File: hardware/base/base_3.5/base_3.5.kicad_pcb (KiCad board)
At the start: 2 copper layers, 82.5 x 17 mm, 9 parts, among them IC1 single_pad_smd, IC2 single_pad_smd, J1 Conn 1, J2 Conn 2

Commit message: base 3.5 update
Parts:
- removed GND (x2): single_pad_smd, cycfi_library:single-pad-3x2
- removed IC1, IC2, OC1, OC2: single_pad_smd, cycfi_library:single-pad-2x2-th
- added J3: Conn_01x03, cycfi_library:xr2-coil-connector, F.Cu at (125.0, 52.0)
- added J4: Conn_01x03, cycfi_library:xr2-coil-connector, F.Cu at (125.0, 58.5)
- moved J2 0.30 mm to (153.1, 55.2)
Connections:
- net /ic2 renamed /OC2
- net /oc1 renamed /OC1
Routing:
- net GND: track 88.3 -> 9.22 mm, vias 6 -> 2
- net /ic1: track 34.3 -> 0.00 mm
- net /OC2: track 10.2 -> 32.6 mm
- net /IC1: track 0.00 -> 10.2 mm
- net /OC1: track 50.5 -> 42.8 mm
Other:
- board size 82.5 x 17 mm -> 82.4 x 17 mm
- board text removed: "IC1"
- board text removed: "IC2"
- board text removed: "OC1"
- board text removed: "OC2"

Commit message: 3.0 and 3.5 base updated
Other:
- board size 82.4 x 17 mm -> 82.5 x 17 mm

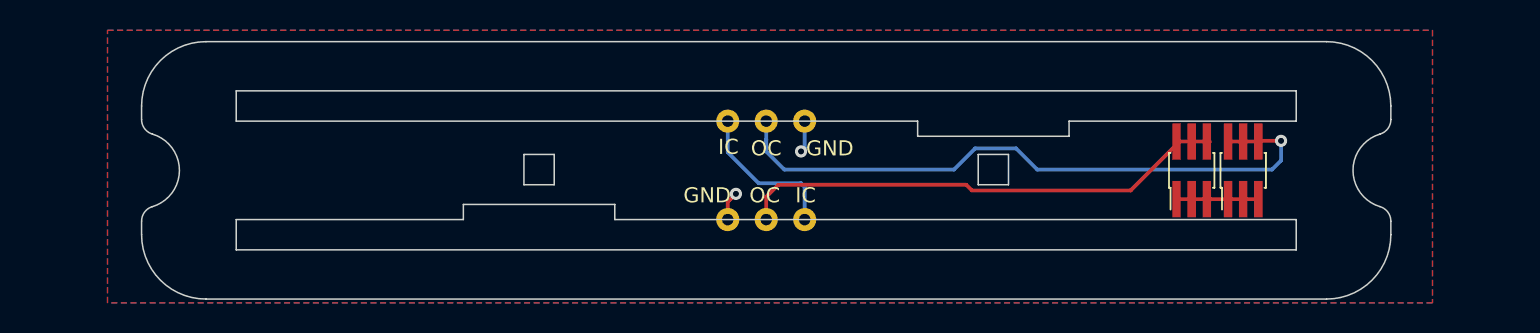
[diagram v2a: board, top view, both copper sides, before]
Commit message: Copied 3.3 to 3.5 and 4.0
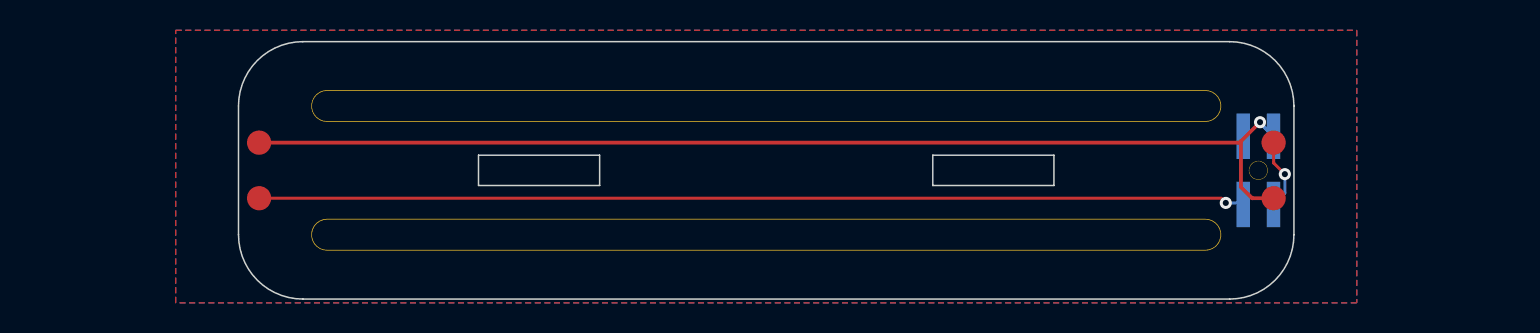
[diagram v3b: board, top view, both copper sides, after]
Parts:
- removed J2: Conn 2, cycfi_library:pin_header_2x3p_1.00mm_smd_vertical
- removed J3, J4: Conn_01x03, cycfi_library:xr2-coil-connector
- added H5: single_pad, xr_spectra_library:rail_slot_3.3, F.Cu at (125.0, 51.0)
- added H6: single_pad, xr_spectra_library:rail_slot_3.3, F.Cu at (125.0, 59.5)
- added IC1: single_pad, cycfi_library:single-pad-1.6x1.6_circular, F.Cu at (91.5, 53.4)
- added IC2: single_pad, cycfi_library:single-pad-1.6x1.6_circular, F.Cu at (158.5, 57.1)
- added OC1: single_pad, cycfi_library:single-pad-1.6x1.6_circular, F.Cu at (158.5, 53.4)
- added OC2: single_pad, cycfi_library:single-pad-1.6x1.6_circular, F.Cu at (91.5, 57.1)
- J1: value Conn 1 -> conn_2x2; footprint cycfi_library:pin_header_2x3p_1.00mm_smd_vertical -> cycfi_library:pin_header_2x2p_2.00mm_smd_vertical; moved to B.Cu
- moved J1 1.00 mm to (157.5, 55.2)
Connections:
- J1 pad 1: GND -> inner_coil
- J1 pad 3: GND -> /out-
- J1 pad 4: /OC1 -> /out+
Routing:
- net inner_coil: track 0.00 -> 73.4 mm, vias 0 -> 1
- net /out-: track 0.00 -> 65.2 mm, vias 0 -> 1
- net /OC1: track 42.8 -> 0.00 mm, vias 1 -> 0
- net /OC2: track 32.6 -> 0.00 mm
- net /IC1: track 10.2 -> 0.00 mm
- net GND: track 9.22 -> 0.00 mm, vias 2 -> 0
- net /out+: track 0.00 -> 4.70 mm, vias 0 -> 1
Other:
- board size 82.5 x 17 mm -> 69.7 x 17 mm
- net class Default removed

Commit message: 3.5" PCB layout
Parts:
- added H1: MountingHole, cycfi_library:hole_3mm, F.Cu at (166.2, 55.2)
- added H2: MountingHole, cycfi_library:hole_3mm, F.Cu at (83.8, 55.2)
- H5, H6: footprint xr_spectra_library:rail_slot_3.3 -> xr_spectra_library:rail_slot_3.5
- moved IC1 6.25 mm to (85.8, 51.0)
- moved OC2 6.24 mm to (85.8, 59.5)
- moved OC1 6.23 mm to (164.2, 51.0)
- moved IC2 6.23 mm to (164.2, 59.5)
- moved J1 5.00 mm to (162.5, 55.2)
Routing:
- net inner_coil: track 73.4 -> 89.6 mm
- net /out-: track 65.2 -> 76.6 mm
- net /out+: track 4.70 -> 7.60 mm
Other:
- board size 69.7 x 17 mm -> 88.9 x 17 mm

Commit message: PCB layout 3.5"
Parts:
- G***: moved to F.Cu
- moved H1 82.5 mm to (83.8, 54.8), turned to 180 degrees
- moved H2 82.5 mm to (166.2, 54.8), turned to 180 degrees
- moved IC1 79.0 mm to (85.8, 50.5), turned to 0 degrees
- moved OC1 79.0 mm to (164.2, 50.5), turned to 0 degrees
- moved IC2 78.9 mm to (164.2, 59.0), turned to 0 degrees
- moved OC2 78.9 mm to (85.8, 59.0), turned to 0 degrees
- moved J1 75.0 mm to (87.5, 54.8), turned to -90 degrees
- moved H6 9.00 mm to (125.0, 50.5)
- moved H5 8.00 mm to (125.0, 59.0)
- moved G*** 0.71 mm to (124.8, 54.8), turned to 0 degrees
- renumbered IC2 to IC1, IC1 to IC2, OC2 to OC1, OC1 to OC2
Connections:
- IC1 pad 1: inner_coil -> /out+
- IC2 pad 1: inner_coil -> /out-
- J1 pad 1: inner_coil -> middle_coil
- OC1 pad 1: /out- -> middle_coil
- OC2 pad 1: /out+ -> middle_coil
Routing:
- net middle_coil: track 0.00 -> 90.4 mm, vias 0 -> 1
- net inner_coil: track 89.6 -> 0.00 mm, vias 1 -> 0
- net /out+: track 7.60 -> 3.49 mm
- net /out-: track 76.6 -> 80.0 mm

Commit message: 3.5" and 3.3" good to go
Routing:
- net /out-: track 80.0 -> 83.8 mm
- net middle_coil: track 90.4 -> 92.6 mm
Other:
- outline, holes or cut-outs redrawn

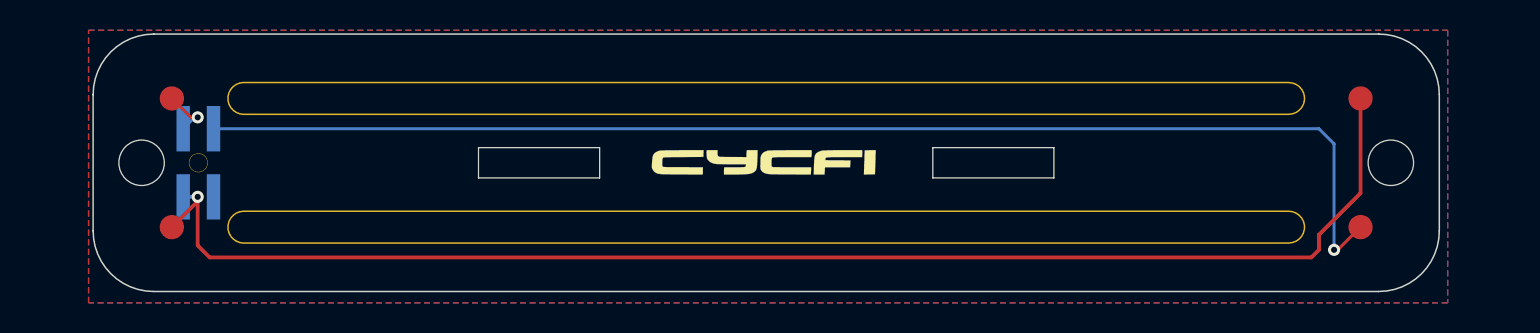
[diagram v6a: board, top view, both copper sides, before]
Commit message: adjusted for proper mouse-bites in panels
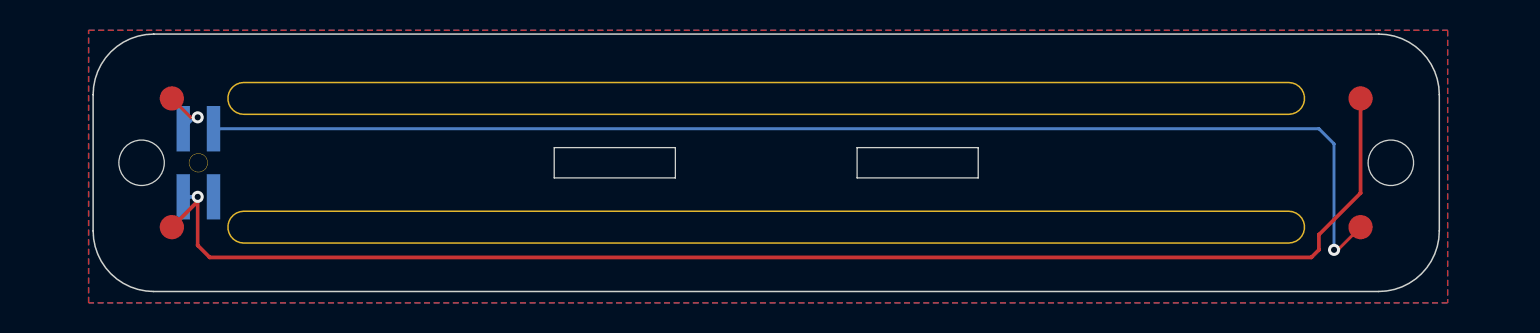
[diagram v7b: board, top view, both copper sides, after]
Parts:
- removed G***: LOGO, cycfi_library:cycfi-logo-15mm
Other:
- outline, holes or cut-outs redrawn
